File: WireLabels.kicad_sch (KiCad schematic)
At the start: 0 parts

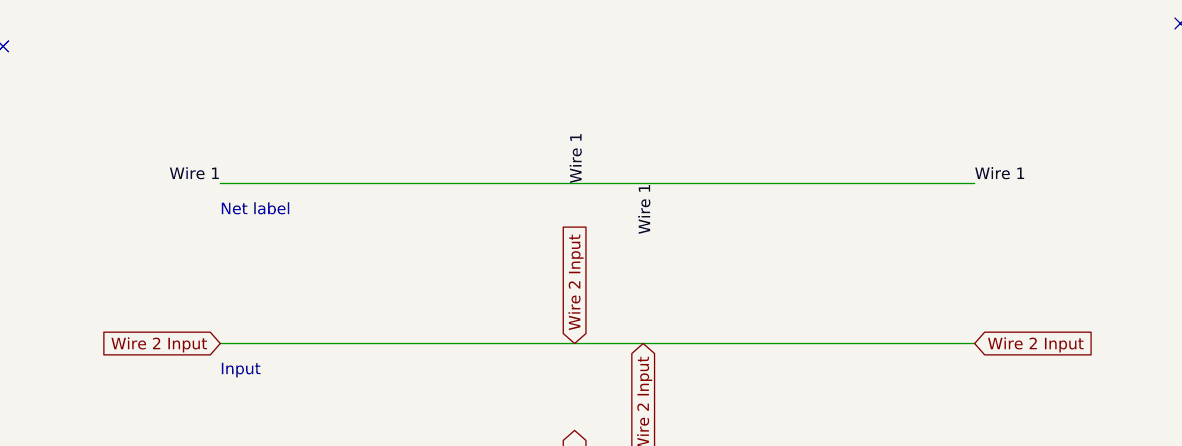
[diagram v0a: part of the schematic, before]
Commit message: add text label annotations for direction
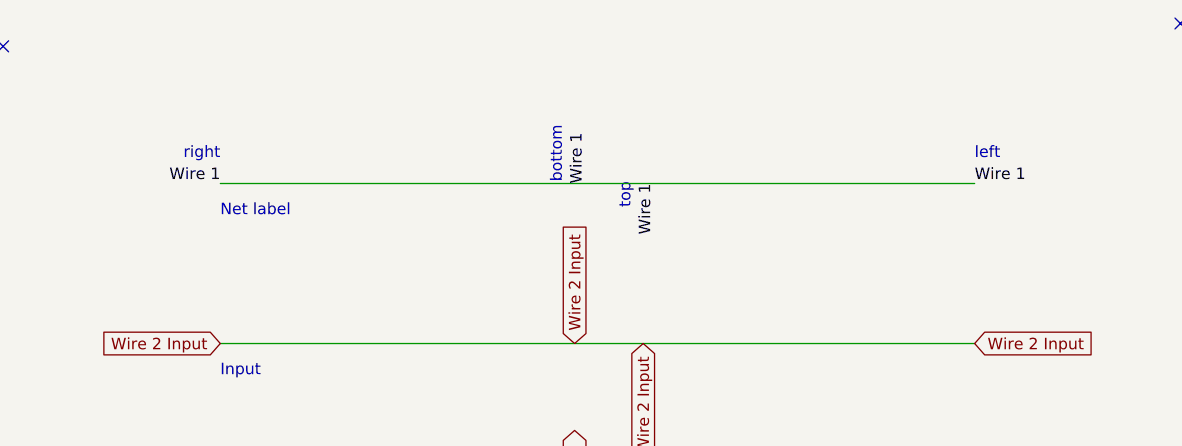
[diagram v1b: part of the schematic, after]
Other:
- note added: "bottom"
- note added: "left"
- note added: "right"
- note added: "top"
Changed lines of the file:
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@@
+    (effects (font (size 1.27 1.27)) (justify left bottom))
+  )
+  (text "bottom" (at 128.27 52.07 90)
     (effects (font (size 1.27 1.27)) (justify left bottom))
   )
   (text "Input" (at 90.17 73.66 0)
     (effects (font (size 1.27 1.27)) (justify left bottom))
+  )
+  (text "top" (at 135.89 52.07 270)
+    (effects (font (size 1.27 1.27)) (justify right bottom))
   )
   (text "Passive" (at 91.44 162.56 0)
@@
     (effects (font (size 1.27 1.27)) (justify left bottom))
   )
+  (text "left" (at 173.99 49.53 0)
+    (effects (font (size 1.27 1.27)) (justify left bottom))
+  )
   (text "Tri-state" (at 90.17 144.78 0)
     (effects (font (size 1.27 1.27)) (justify left bottom))
   )
+  (text "right" (at 90.17 49.53 180)
+    (effects (font (size 1.27 1.27)) (justify right bottom))
+  )
   (label "Wire 1" (at 138.43 52.07 270)
